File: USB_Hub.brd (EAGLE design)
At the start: 90 x 36 mm, 53 parts, among them CON1 USB-ZX62, CON2 USB-5075AR-04-WH, CON3 USB-5075AR-04-WH, CON4 USB-5075AR-04-WH, CON5 USB-5075AR-04-WH, IC1 UPC720115, IC2 AP22652, J1 VBUS, J2 BUS/SELF, SW1 RESET, X1 24MHz

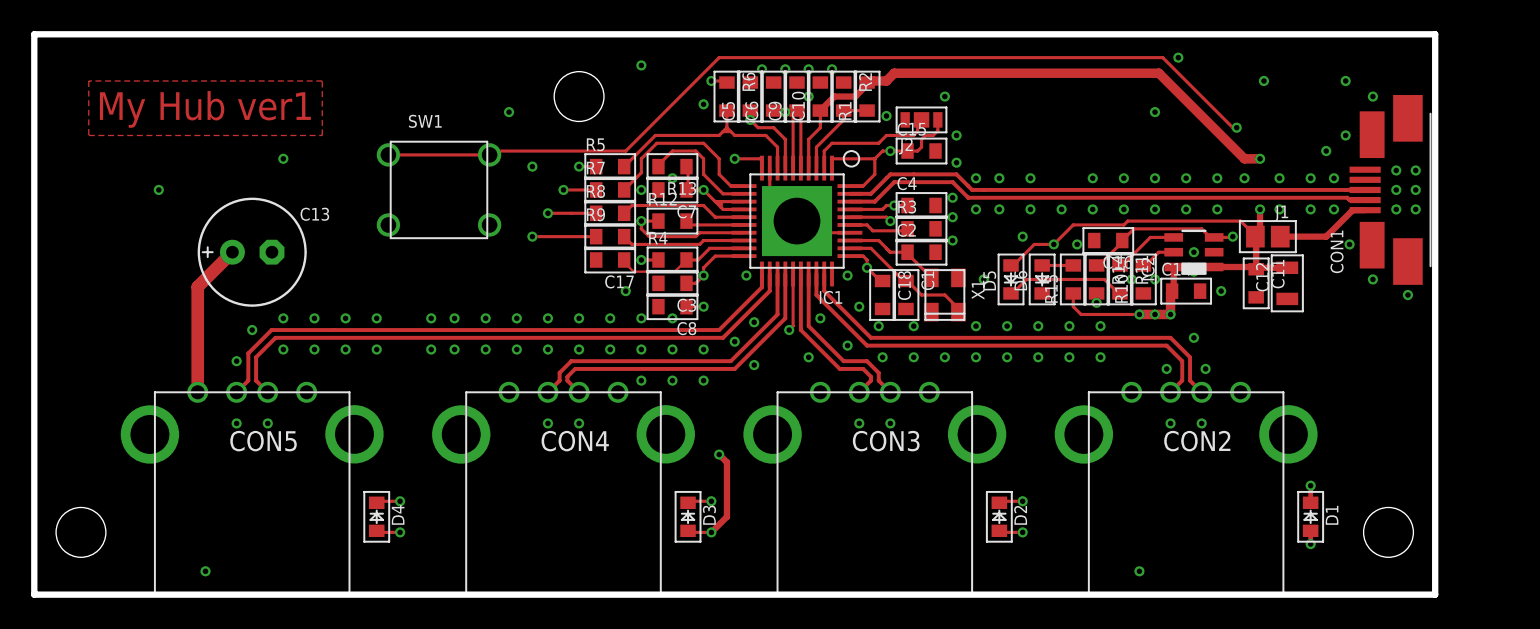
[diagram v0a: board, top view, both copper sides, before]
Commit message: 電圧確認用のポートを追加
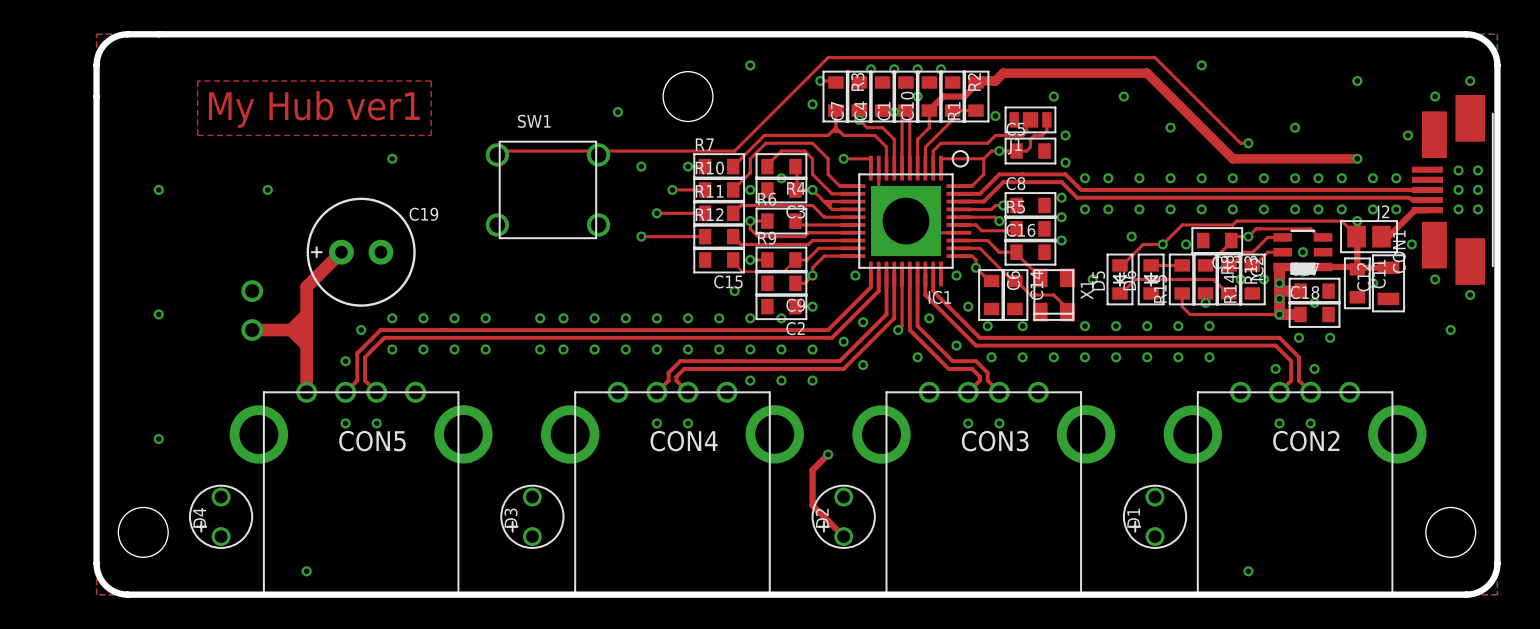
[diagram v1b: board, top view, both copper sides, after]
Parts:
- added C19: 220u, my_rcl:E2.5-6.5
- added TP1: BUS, my_connector:TESTPIN
- added TP2: GND, my_connector:TESTPIN
- C1: value 10p -> 10u
- C13: value 220u -> 1u; device my_rcl:E2.5-6.5 -> my_rcl:1608
- C14, C16: value 1u -> 10p
- C15, C18: value 0.1u -> 1u
- C2: value 10p -> 0.1u
- C5, C9: value 10u -> 0.1u
- C7: value 0.1u -> 10u
- D1, D2, D3, D4: device my_rcl:D1608 -> my_rcl:LED2.5
- IC1: value UPC720115 -> UPD720115
- J1: value VBUS -> BUS/SELF; device my_rcl:2012-J -> my_rcl:1608-3-J
- J2: value BUS/SELF -> VBUS; device my_rcl:1608-3-J -> my_rcl:2012-J
- R10: value 25k -> 1k
- R11: value 1.5k -> 1k
- R12: value 10k -> 1k
- R13: value 10k -> 1.5k
- R14: value 10k -> 25k
- R3: value 1.6k -> 10k
- R5: value 1k -> 1.6k
- R8, R9: value 1k -> 10k
- moved C13 62.0 mm to (72.0, 22.8), turned to 180 degrees
- moved C17 45.3 mm to (78.2, 19.5), turned to 0 degrees
- moved R8 38.5 mm to (71.2, 20.2), turned to 270 degrees
- moved R13 36.5 mm to (72.8, 20.2), turned to 270 degrees
- moved J2 29.7 mm to (81.8, 23.0), turned to 180 degrees
- moved R10 27.9 mm to (40.0, 26.0), turned to 0 degrees
- moved C18 27.8 mm to (78.2, 18.0), turned to 0 degrees
- moved R5 27.3 mm to (60.0, 23.5)
- moved R11 26.1 mm to (40.0, 24.5), turned to 0 degrees
- moved C8 23.9 mm to (60.0, 25.0), turned to 0 degrees
- moved C6 18.9 mm to (57.5, 19.2), turned to 270 degrees
- moved C5 18.3 mm to (60.0, 28.5), turned to 0 degrees
- moved J1 17.0 mm to (60.0, 30.5), turned to 0 degrees
- moved C15 14.8 mm to (40.0, 21.5), turned to 180 degrees
- moved C7 13.4 mm to (49.0, 32.0), turned to 90 degrees
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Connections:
- net +1V0: now also C7.1, C8.1, C9.1; no longer C3.1, C4.1, C5.1
- net +3V3: now also C1.1, C2.1, C3.1, C4.1, C5.1, J1.3, R3.1, R9.1; no longer C15.1, C18.1, C7.1, C8.1, C9.1, J2.3, R12.1, R13.1
- net +5V: now also J2.2, R8.2; no longer J1.2, R14.2
- net GND: now also C13.2, C19.-, J1.1, R14.1, R5.2, TP2.1; no longer C13.-, J2.1, R10.1, R3.2
- net LED1: now also R3.2, R7.2; no longer R5.2, R6.2
- net LED2: now also R10.2; no longer R7.2
- net LED3: now also R11.2; no longer R8.2
- net LED4: now also R12.2; no longer R9.2
- net N$1: now also J2.1; no longer J1.1
- net N$10: now also R11.1; no longer R8.1
- net N$11: now also R12.1; no longer R9.1
- net N$12: now also R13.1; no longer R11.1
- net N$13: now also R14.2; no longer R10.2
- net N$14: now also R6.2; no longer R12.2
- net N$15: now also R4.2; no longer R13.2
- net N$17: now also J1.2; no longer J2.2
- net N$2: now also R13.2; no longer R11.2
- net N$4: now also R5.1; no longer R3.1
- net N$5: now also C14.1; no longer C1.1
- net N$6: now also C16.1; no longer C2.1
- net N$7: now also C15.1, R9.2; no longer C17.1, R4.2
- net N$8: now also R7.1; no longer R5.1
- net N$9: now also R10.1; no longer R7.1
- net USB_+5V: now also C17.1, C18.1, C19.+, TP1.1; no longer C13.+, C14.1
- net VBUS_EN: now also C13.1, R8.1; no longer C16.1, R14.1
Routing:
- net N$9: track 69.9 -> 49.2 mm, vias 2 -> 1
- net N$10: track 50.0 -> 29.9 mm, vias 2 -> 1
- net N$8: track 87.5 -> 69.1 mm, vias 2 -> 1
- net N$11: track 30.1 -> 45.1 mm, vias 2 -> 1
- net USB_+5V: track 114.8 -> 124.7 mm
- net VBUS_EN: track 76.1 -> 68.1 mm
- net +3V3: track 182.8 -> 179.4 mm, vias 16 -> 12
- net USB_DPU: track 34.0 -> 31.0 mm
- net USB_DMU: track 34.1 -> 31.1 mm
- net N$1: track 6.15 -> 3.65 mm
- net +5V: track 71.0 -> 68.6 mm
- net GND: vias 138 -> 145
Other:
- outline, holes or cut-outs redrawn

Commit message: Type-Cに変更
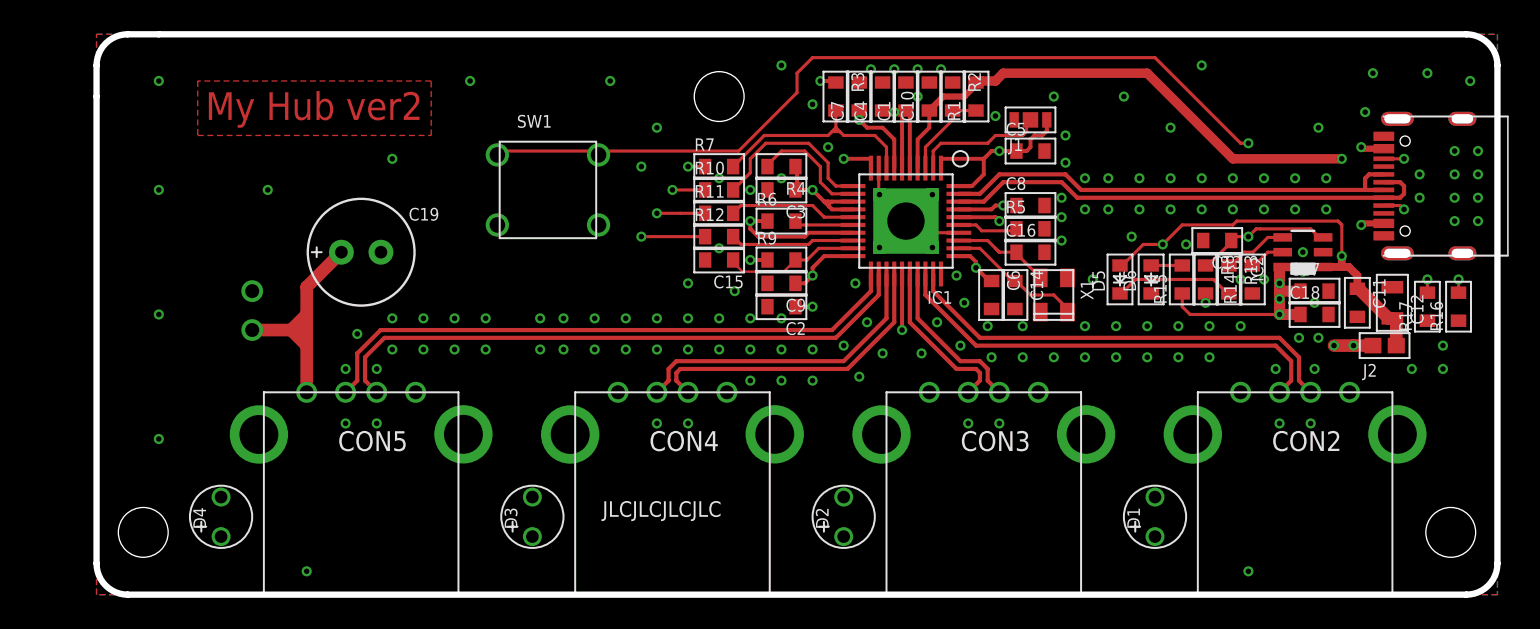
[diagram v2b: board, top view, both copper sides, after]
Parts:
- added R16, R17: 5k, my_rcl:1608
- C14, C16: value 10p -> 22p
- CON1: value USB-ZX62 -> USB-C; device my_connector:ZX62-AB-5PA -> my_connector:5077CR-16-SMC2-BK-TR
- J2: device my_rcl:2012-J -> my_rcl:1608-J
- R14: value 25k -> 20k
- moved J2 7.07 mm to (82.8, 16.0), turned to 0 degrees
- moved CON1 2.51 mm to (83.0, 26.2)
- moved DR3 2.00 mm to (40.0, 32.0)
- moved C12 1.27 mm to (83.2, 18.8), turned to 90 degrees
- moved C11 1.25 mm to (81.0, 18.8)
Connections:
- new net N$18: CON1.B5:CC2, R16.2
- new net N$19: CON1.A5:CC1, R17.2
- net GND: now also CON1.A1,B12:GND, CON1.B1,A12:GND, CON1.SHILED1, CON1.SHILED2, CON1.SHILED3, CON1.SHILED4, CON1.SHILED5, CON1.SHILED6, CON1.SHILED7, CON1.SHILED8, IC1.HT1, IC1.HT2, IC1.HT3, IC1.HT4, R16.1, R17.1; no longer CON1.5, CON1.M1, CON1.M2, CON1.M3, CON1.M4
- net N$1: now also CON1.A4,B9:VBUS, CON1.B4,A9:VBUS; no longer CON1.1
- net USB_DMU: now also CON1.A7:DN1, CON1.B7:DN2; no longer CON1.2
- net USB_DPU: now also CON1.A6:DP1, CON1.B6:DP2; no longer CON1.3
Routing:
- net +3V3: track 179.4 -> 199.3 mm, vias 12 -> 11
- net N$1: track 3.65 -> 19.7 mm, vias 0 -> 4
- net N$18: track 0.00 -> 12.2 mm, vias 0 -> 2
- net N$19: track 0.00 -> 7.81 mm, vias 0 -> 2
- net +5V: track 68.6 -> 72.0 mm
- net USB_DPU: track 31.0 -> 30.3 mm
- net VBUS_EN: track 68.1 -> 68.9 mm
- net GND: vias 145 -> 151
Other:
- board text added: "JLCJLCJLCJLC"
- board text added: "My Hub ver2"
- board text removed: "My Hub ver1"
